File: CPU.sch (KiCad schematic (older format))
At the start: 13 parts, among them J4 Conn_01x03_Male, U1 STM32F405RGTx, Y1 8MHz

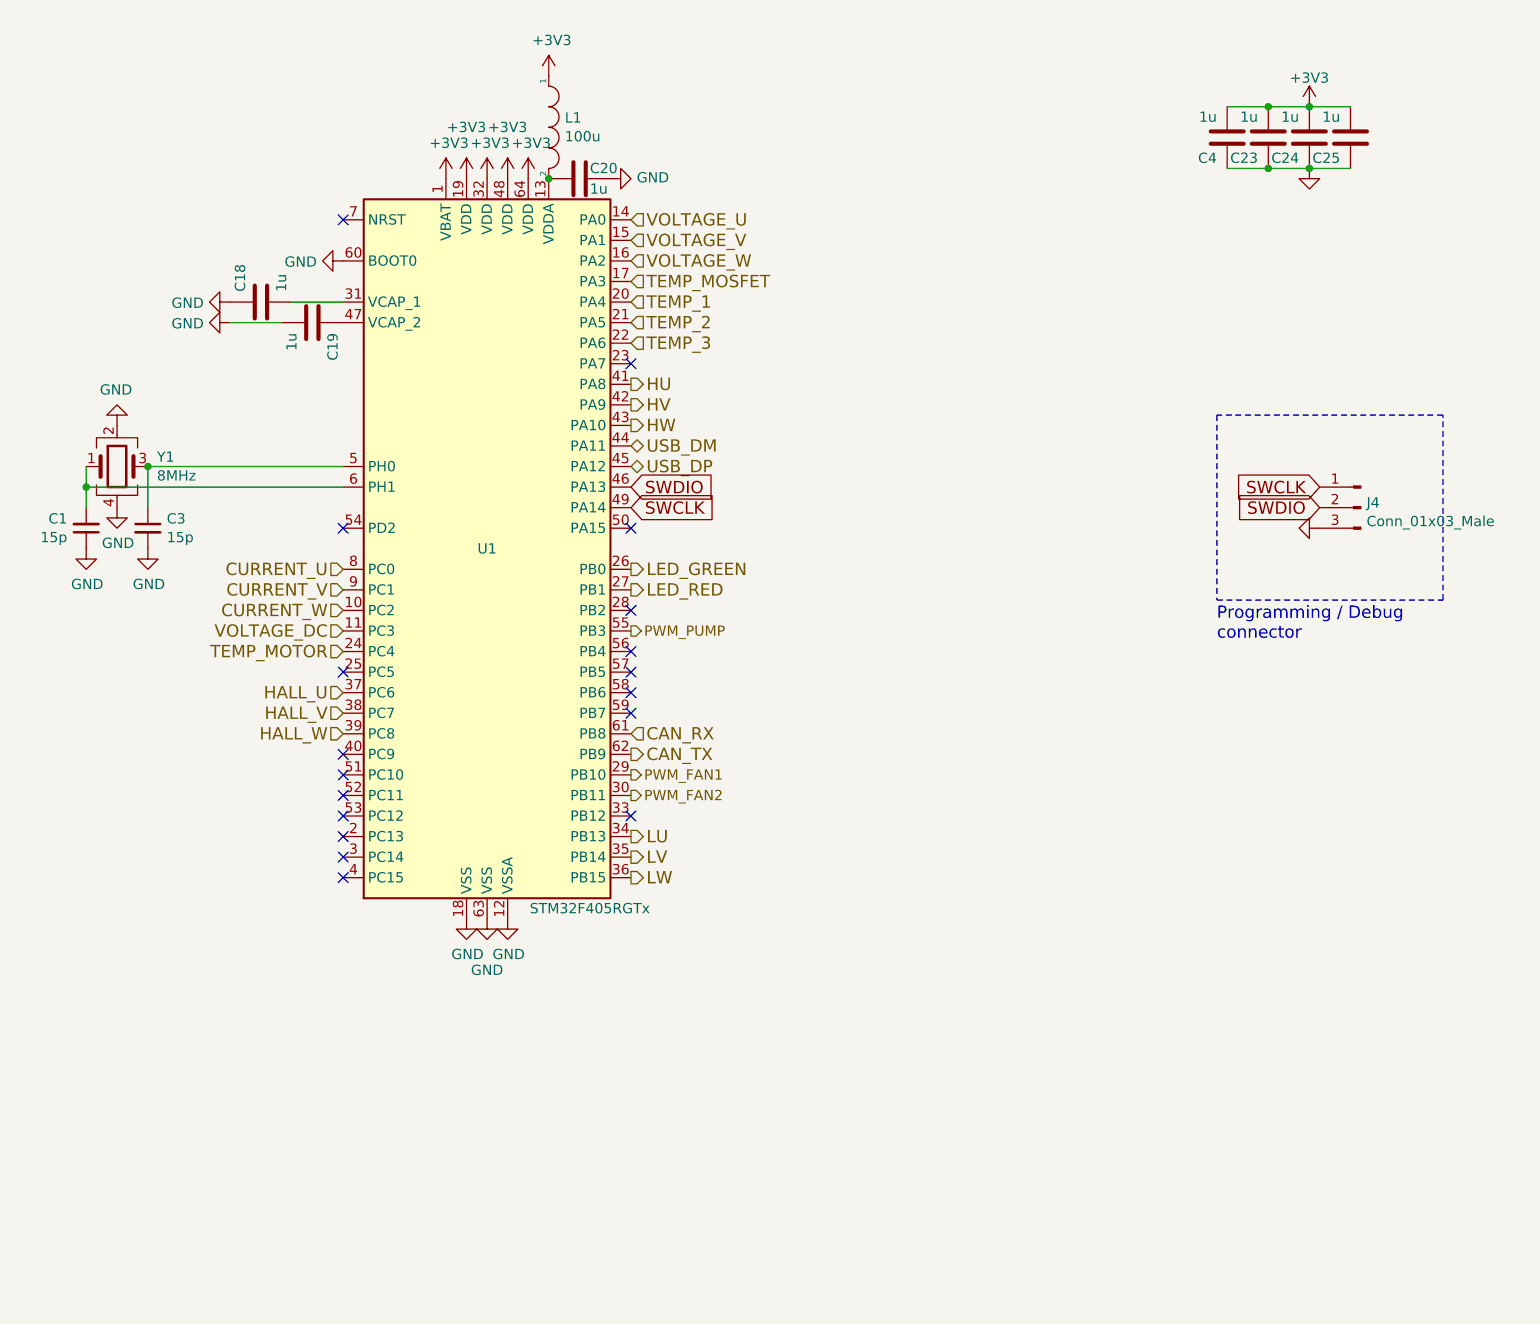
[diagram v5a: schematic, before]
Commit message: - removed Temp3 input - removed hall input - removed CAN - added HMI UART - added freewheeling diode to pump output - moved temp connector left to mitigate collision with USB - added fourth pinhole for pasting
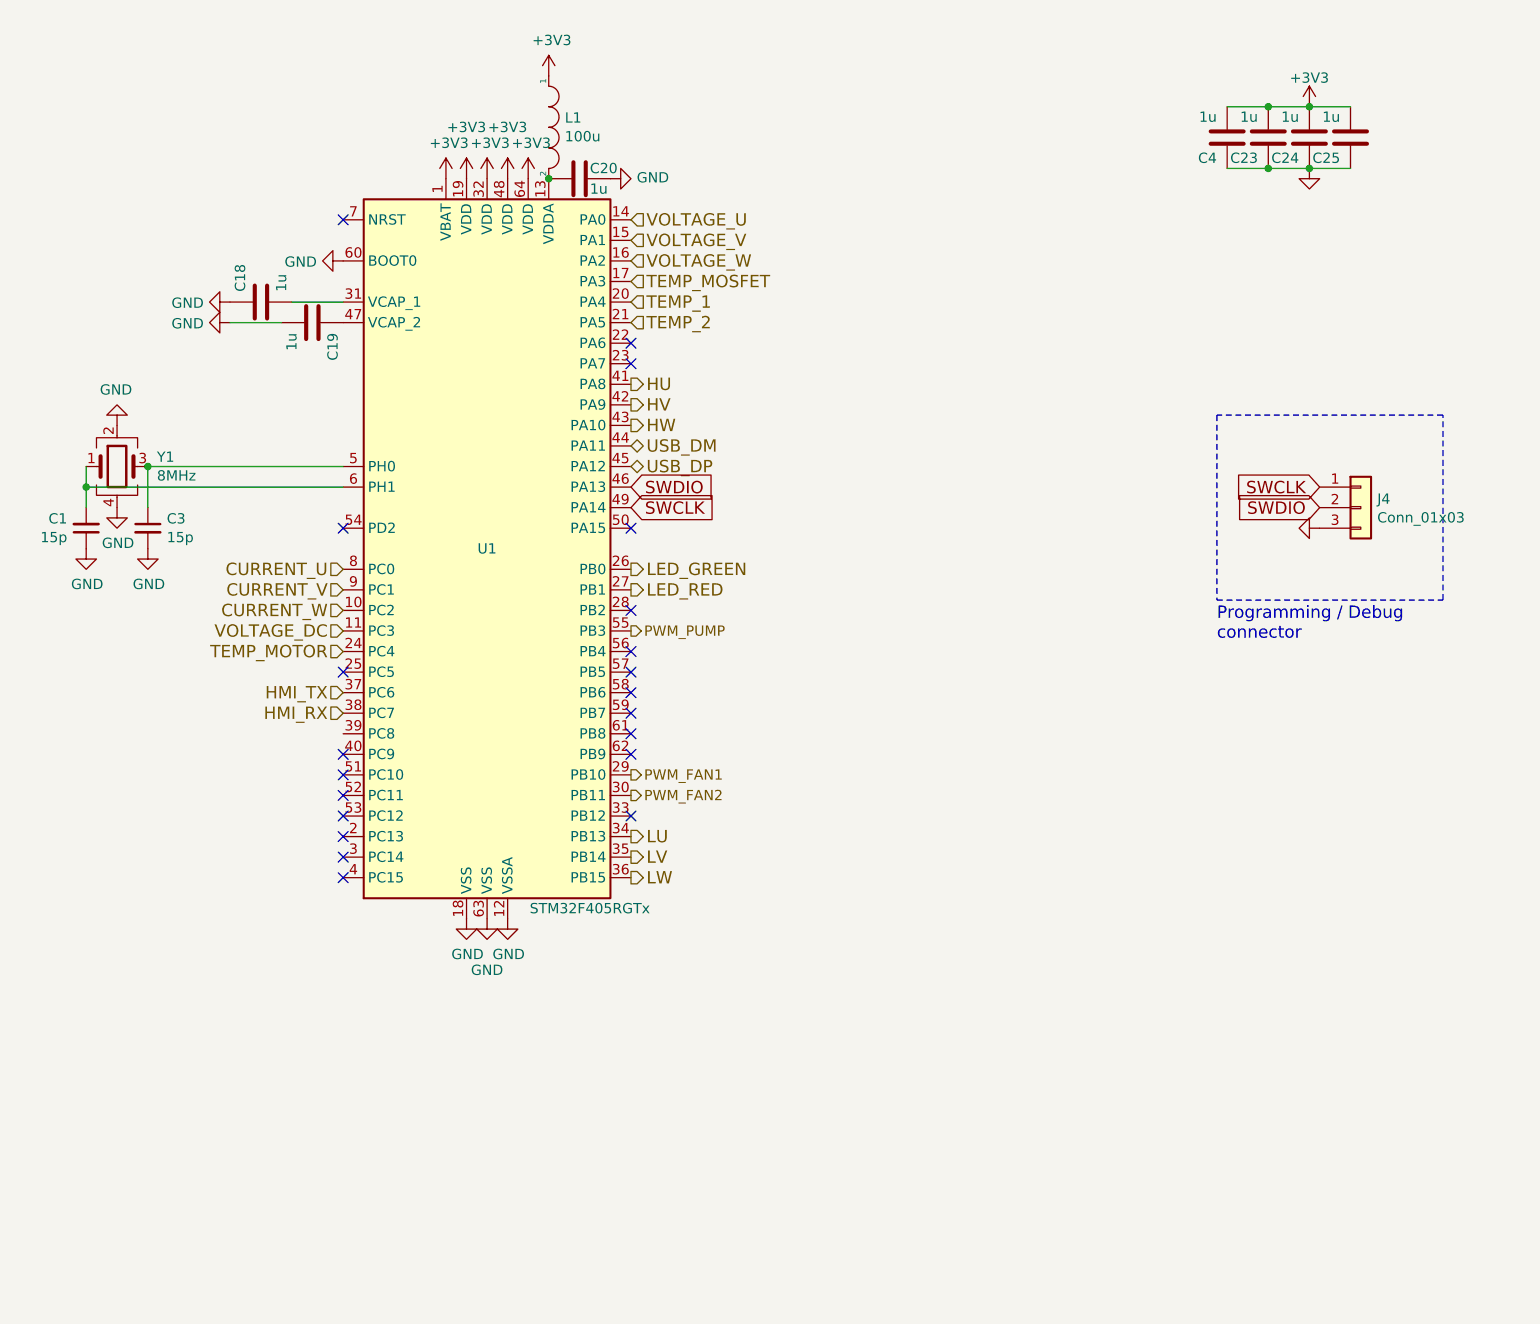
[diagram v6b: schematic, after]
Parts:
- removed J4: Conn_01x03_Male, Connector_PinHeader_2.00mm:PinHeader_1x03_P2.00mm_Vertical, symbol Connector:Conn_01x03_Male
- added J4: Conn_01x03, Connector_PinHeader_2.00mm:PinHeader_1x03_P2.00mm_Vertical, symbol Connector_Generic:Conn_01x03
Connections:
- net GND: now also J4.3 (Pin_3)
- net SWCLK: now also J4.1 (Pin_1)
- net SWDIO: now also J4.2 (Pin_2)
- net CAN_RX: no longer names the net of U1.61 (PB8)
- net CAN_TX: no longer names the net of U1.62 (PB9)
- net HALL_U renamed HMI_TX
- net HALL_V renamed HMI_RX
- net HALL_W: no longer names the net of U1.39 (PC8)
- net TEMP_3: no longer names the net of U1.22 (PA6)
- no-connect marks 18 -> 21
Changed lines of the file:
@@
 USB_DP
 Text HLabel 5000 4000 0    60   Input ~ 0
-HALL_U
+HMI_TX
 Text HLabel 5000 4100 0    60   Input ~ 0
-HALL_V
+HMI_RX
 Text HLabel 5000 3800 0    60   Input ~ 0
 TEMP_MOTOR
@@
 EndData
 $EndBitmap
-Text HLabel 6400 4200 2    60   Input ~ 0
-CAN_RX
-Text HLabel 6400 4300 2    60   Output ~ 0
-CAN_TX
 Text HLabel 6400 3500 2    60   Output ~ 0
 LED_RED
 Text HLabel 6400 3400 2    60   Output ~ 0
 LED_GREEN
-Text HLabel 6400 2300 2    60   Input ~ 0
-TEMP_3
 Text HLabel 6400 2000 2    60   Input ~ 0
 TEMP_MOSFET
@@
 Text HLabel 5000 3600 0    60   Input ~ 0
 CURRENT_W
-Text HLabel 5000 4200 0    60   Input ~ 0
-HALL_W
 $Comp
 L power:GND #PWR0101
@@
 Connection ~ 9500 1150
 Connection ~ 9500 1450
+NoConn ~ 5000 1700
+NoConn ~ 6400 2300
+NoConn ~ 6400 4200
+NoConn ~ 6400 4300
 $Comp
-L Connector:Conn_01x03_Male J4
-U 1 1 5FAC96B0
+L Connector_Generic:Conn_01x03 J4
+U 1 1 5FDFFCD8
 P 9950 3100
-F 0 "J4" H 9922 3124 50  0000 R CNN
-F 1 "Conn_01x03_Male" H 9922 3033 50  0000 R CNN
+F 0 "J4" H 10030 3142 50  0000 L CNN
+F 1 "Conn_01x03" H 10030 3051 50  0000 L CNN
 F 2 "Connector_PinHeader_2.00mm:PinHeader_1x03_P2.00mm_Vertical" H 9950 3100 50  0001 C CNN
 F 3 "~" H 9950 3100 50  0001 C CNN
 	1    9950 3100
-	-1   0    0    -1
+	1    0    0    -1
 $EndComp
-NoConn ~ 5000 1700
 $EndSCHEMATC

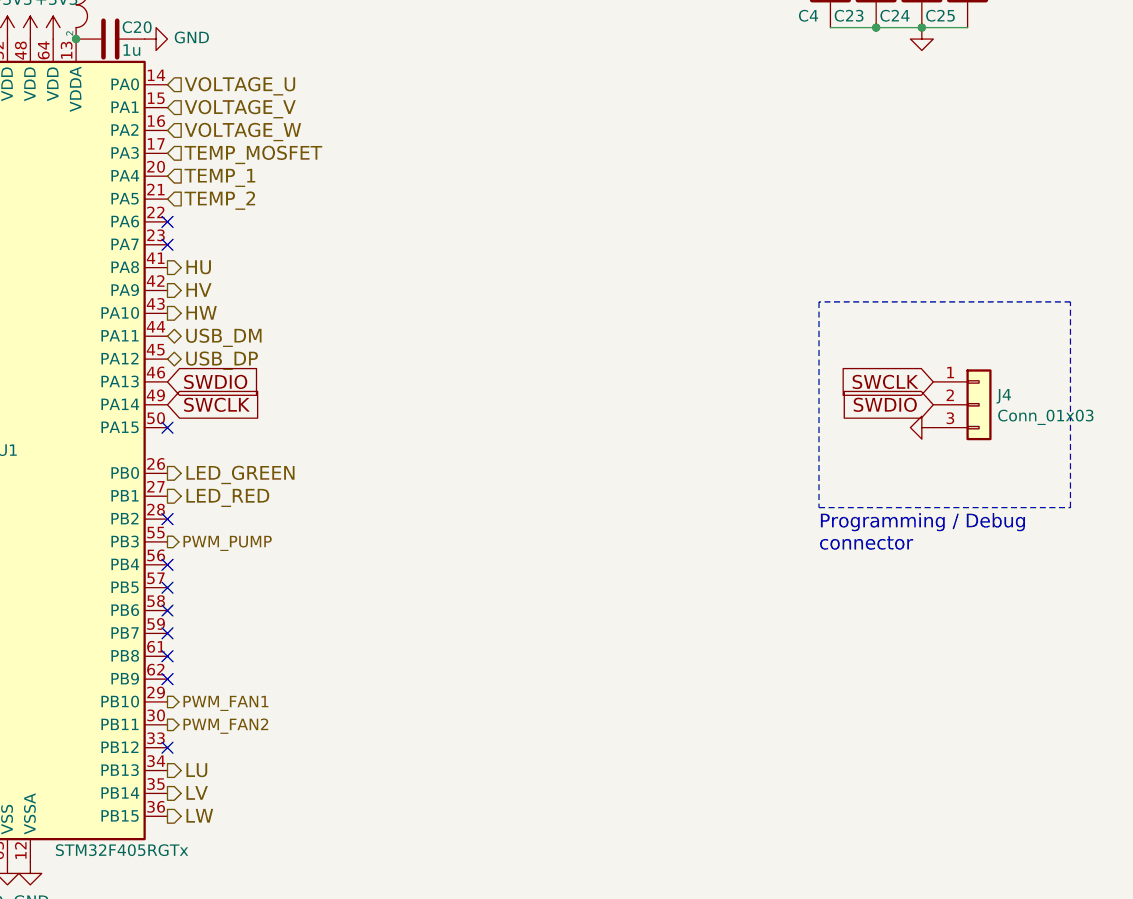
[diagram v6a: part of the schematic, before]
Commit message: - removed one fan output - moved PWM pins to TIM4 - added pull-up to fan output (for 4pin fan) - removed blue power LED - split 12pin to 5 2pin connectors - reduced LED resistors - removed optional current sensor - removed HV DCDC converter - added some cap values
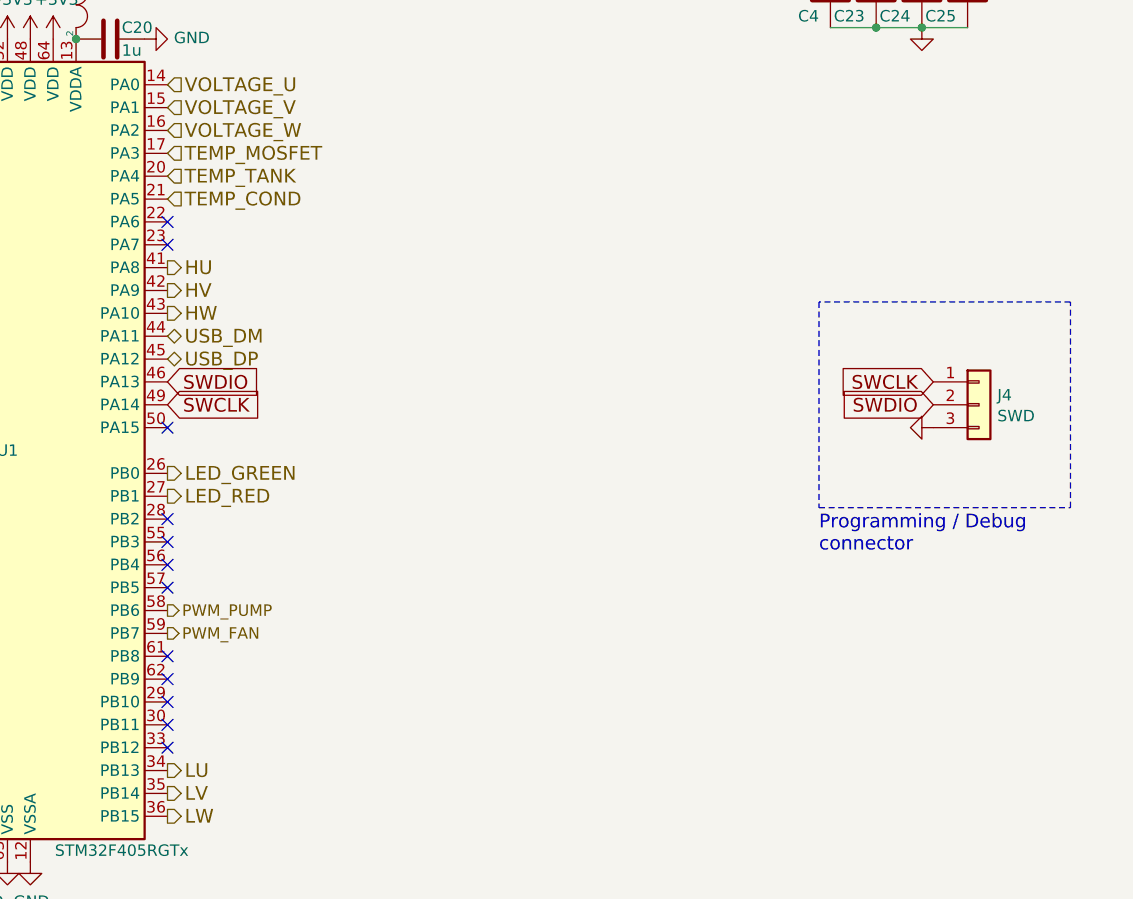
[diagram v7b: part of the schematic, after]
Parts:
- J4: value Conn_01x03 -> SWD; footprint Connector_PinHeader_2.00mm:PinHeader_1x03_P2.00mm_Vertical -> Connector_JST:JST_PH_B3B-PH-K_1x03_P2.00mm_Vertical
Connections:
- net PWM_PUMP: now also U1.58 (PB6); no longer U1.55 (PB3)
- net PWM_FAN: now reaches U1.59 (PB7)
- net PWM_FAN1: no longer names the net of U1.29 (PB10)
- net PWM_FAN2: no longer names the net of U1.30 (PB11)
- net TEMP_1 renamed TEMP_TANK
- net TEMP_2 renamed TEMP_COND
- no-connect marks 21 -> 22
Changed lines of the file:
@@
 LU
 Text HLabel 6400 2200 2    60   Input ~ 0
-TEMP_2
+TEMP_COND
 Text HLabel 6400 2500 2    60   Output ~ 0
 HU
@@
 TEMP_MOSFET
 Text HLabel 6400 2100 2    60   Input ~ 0
-TEMP_1
+TEMP_TANK
 $Comp
 L power:+3V3 #PWR051
@@
 NoConn ~ 6400 3800
 NoConn ~ 6400 3900
-NoConn ~ 6400 4000
-NoConn ~ 6400 4100
 NoConn ~ 6400 4600
 NoConn ~ 5000 3900
@@
 	1    0    0    -1
 $EndComp
-Text HLabel 6400 3700 2    50   Output ~ 0
+Text HLabel 6400 4000 2    50   Output ~ 0
 PWM_PUMP
 NoConn ~ 6400 2400
-Text HLabel 6400 4400 2    50   Output ~ 0
-PWM_FAN1
-Text HLabel 6400 4500 2    50   Output ~ 0
-PWM_FAN2
+Text HLabel 6400 4100 2    50   Output ~ 0
+PWM_FAN
 Connection ~ 9500 1150
 Connection ~ 9500 1450
@@
 P 9950 3100
 F 0 "J4" H 10030 3142 50  0000 L CNN
-F 1 "Conn_01x03" H 10030 3051 50  0000 L CNN
-F 2 "Connector_PinHeader_2.00mm:PinHeader_1x03_P2.00mm_Vertical" H 9950 3100 50  0001 C CNN
+F 1 "SWD" H 10030 3051 50  0000 L CNN
+F 2 "Connector_JST:JST_PH_B3B-PH-K_1x03_P2.00mm_Vertical" H 9950 3100 50  0001 C CNN
 F 3 "~" H 9950 3100 50  0001 C CNN
 	1    9950 3100
 	1    0    0    -1
 $EndComp
+NoConn ~ 6400 4500
+NoConn ~ 6400 4400
+NoConn ~ 6400 3700
 $EndSCHEMATC
